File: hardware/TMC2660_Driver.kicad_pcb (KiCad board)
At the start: 4 copper layers, 36.7 x 39.4 mm, 30 parts, among them J1 PCIe_Stepper, J2 Conn_01x04_Male, U1 TMC2660, U2 74LVC1G06, U3 24LC02

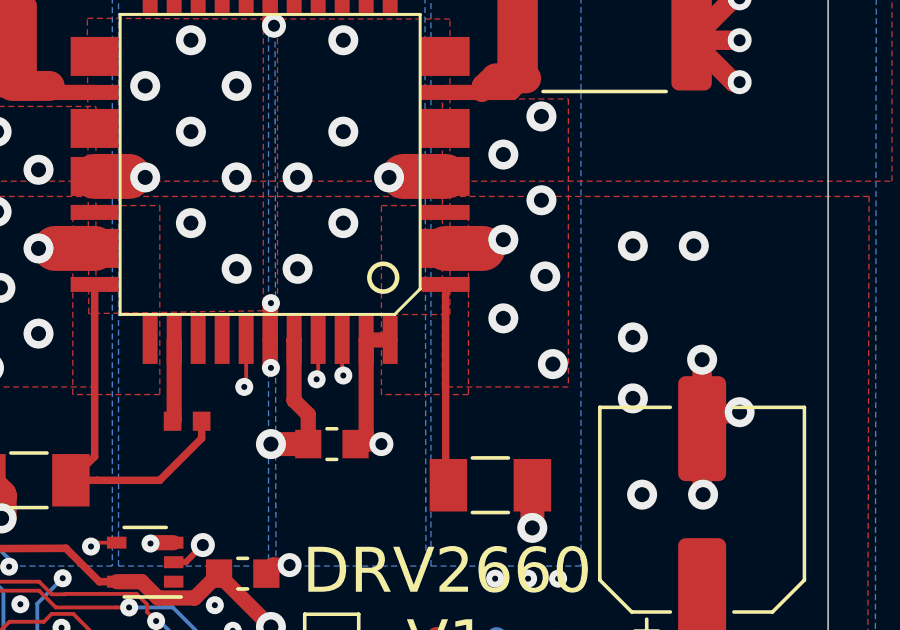
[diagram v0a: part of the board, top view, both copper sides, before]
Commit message: Updated DRC rules. Fix labels.
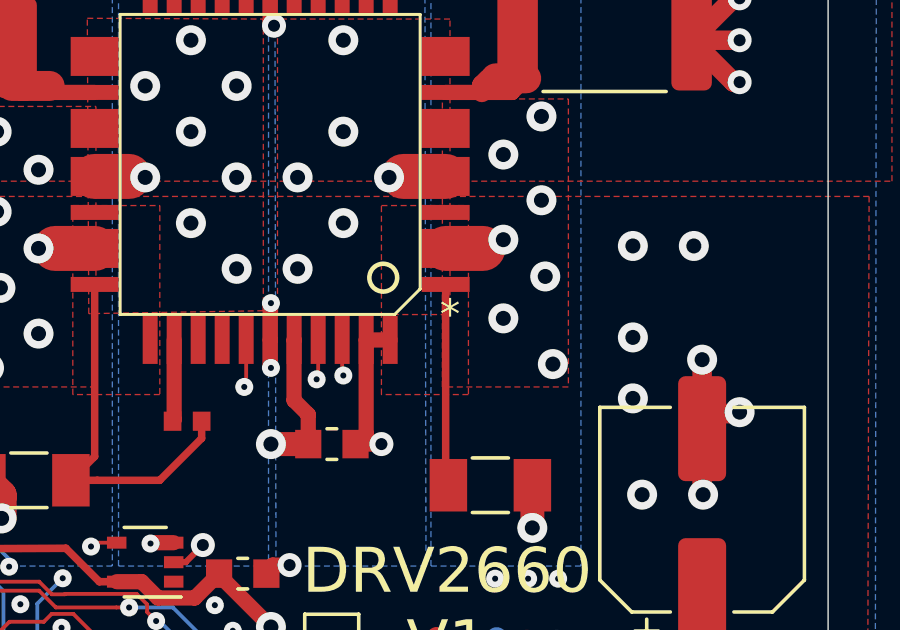
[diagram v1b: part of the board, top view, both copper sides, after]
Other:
- board text added: "(c) iQury.us Nov 2020"
- board text removed: "(c) iQury.us May 2020"
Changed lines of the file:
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@@
     (pcbplotparams
       (layerselection 0x00010fc_ffffffff)
+      (disableapertmacros false)
       (usegerberextensions true)
       (usegerberattributes false)
@@
       (svgprecision 6)
       (excludeedgelayer true)
-      (linewidth 0.100000)
       (plotframeref false)
       (viasonmask false)
@@
   (gr_arc (start 113.6 113) (end 113.6 114) (angle -90) (layer "Edge.Cuts") (width 0.05))
   (gr_line (start 117.5 114) (end 127.7 114) (layer "Edge.Cuts") (width 0.05))
-  (gr_text "(c) iQury.us\nMay 2020" (at 143.637 93 90) (layer "B.SilkS")
+  (gr_text "(c) iQury.us\nNov 2020" (at 143.637 93 90) (layer "B.SilkS")
     (effects (font (size 1 1) (thickness 0.15)) (justify mirror))
   )
@@
     (effects (font (size 1.5 1.5) (thickness 0.3)))
   )
+  (gr_text "*" (at 133.096 94.996) (layer "F.SilkS")
+    (effects (font (size 1 1) (thickness 0.15)))
+  )
   (gr_text "*" (at 115.33 100.254) (layer "F.SilkS")

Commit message: Update 2660 and 2130 driver fab files.
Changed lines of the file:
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@@
     (fp_line (start -3.15 -1.6) (end 3.15 -1.6) (layer "F.Fab") (width 0.1))
     (fp_line (start -3.15 1.6) (end -3.15 -1.6) (layer "F.Fab") (width 0.1))
-    (pad "1" smd roundrect (at -2.9 0 180) (size 1.35 3.35) (layers "F.Cu" "F.Paste" "F.Mask") (roundrect_rratio 0.185185)
+    (pad "1" smd roundrect (at -2.9 0 180) (size 1.35 3.35) (layers "F.Cu" "F.Paste" "F.Mask") (roundrect_rratio 0.1851851851851852)
       (net 17 "Net-(R1-Pad2)"))
-    (pad "2" smd roundrect (at 2.9 0 180) (size 1.35 3.35) (layers "F.Cu" "F.Paste" "F.Mask") (roundrect_rratio 0.185185)
+    (pad "2" smd roundrect (at 2.9 0 180) (size 1.35 3.35) (layers "F.Cu" "F.Paste" "F.Mask") (roundrect_rratio 0.1851851851851852)
       (net 2 "GND"))
     (model "${KISYS3DMOD}/Resistor_SMD.3dshapes/R_2512_6332Metric.wrl"
@@
     (fp_line (start -3.15 -1.6) (end 3.15 -1.6) (layer "F.Fab") (width 0.1))
     (fp_line (start 3.15 1.6) (end -3.15 1.6) (layer "F.Fab") (width 0.1))
-    (pad "1" smd roundrect (at -2.9 0) (size 1.35 3.35) (layers "F.Cu" "F.Paste" "F.Mask") (roundrect_rratio 0.185185)
+    (pad "1" smd roundrect (at -2.9 0) (size 1.35 3.35) (layers "F.Cu" "F.Paste" "F.Mask") (roundrect_rratio 0.1851851851851852)
       (net 18 "Net-(R3-Pad2)"))
-    (pad "2" smd roundrect (at 2.9 0) (size 1.35 3.35) (layers "F.Cu" "F.Paste" "F.Mask") (roundrect_rratio 0.185185)
+    (pad "2" smd roundrect (at 2.9 0) (size 1.35 3.35) (layers "F.Cu" "F.Paste" "F.Mask") (roundrect_rratio 0.1851851851851852)
       (net 2 "GND"))
     (model "${KISYS3DMOD}/Resistor_SMD.3dshapes/R_2512_6332Metric.wrl"

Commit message: Generate fabrication files for Rev 5.
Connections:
- net /~CS renamed /~{CS}
- net /~ENABLE renamed /~{ENABLE}

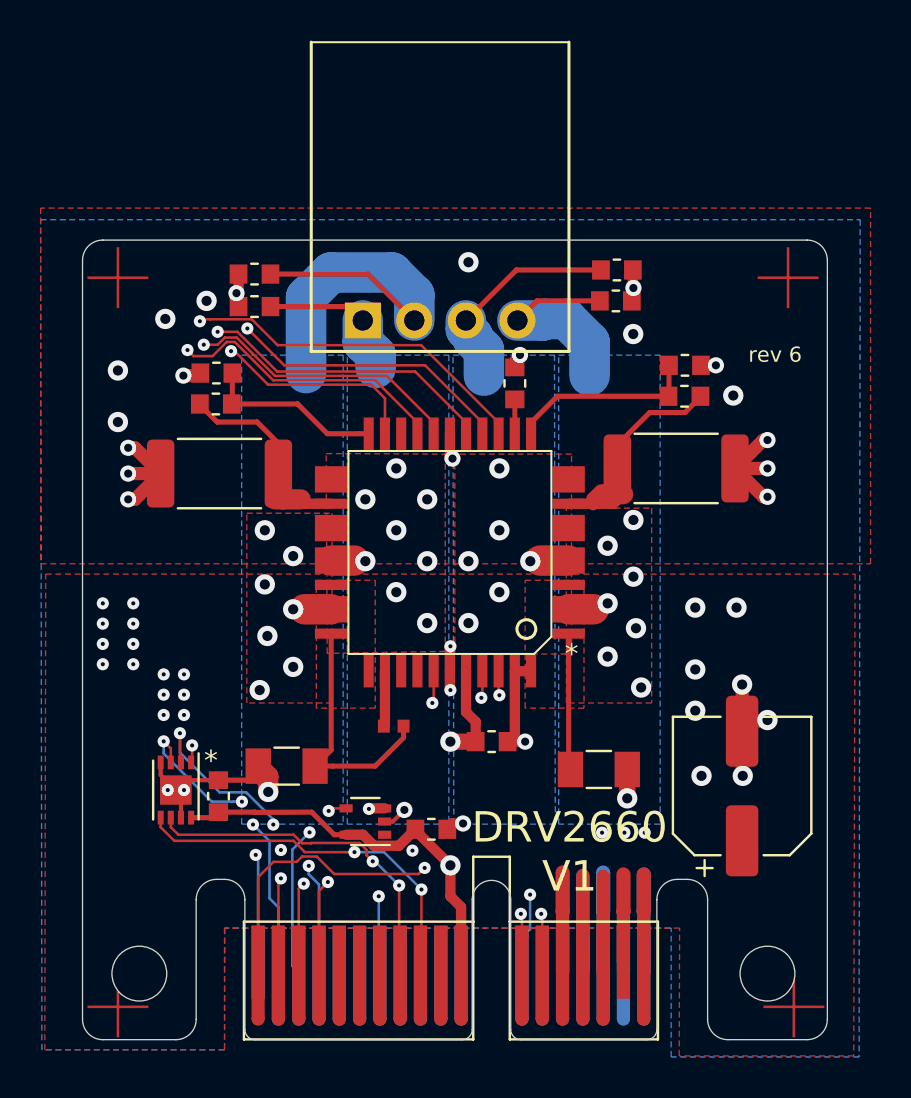
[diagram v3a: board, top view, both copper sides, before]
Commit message: Update drivers to respect high motor coltage circuit.
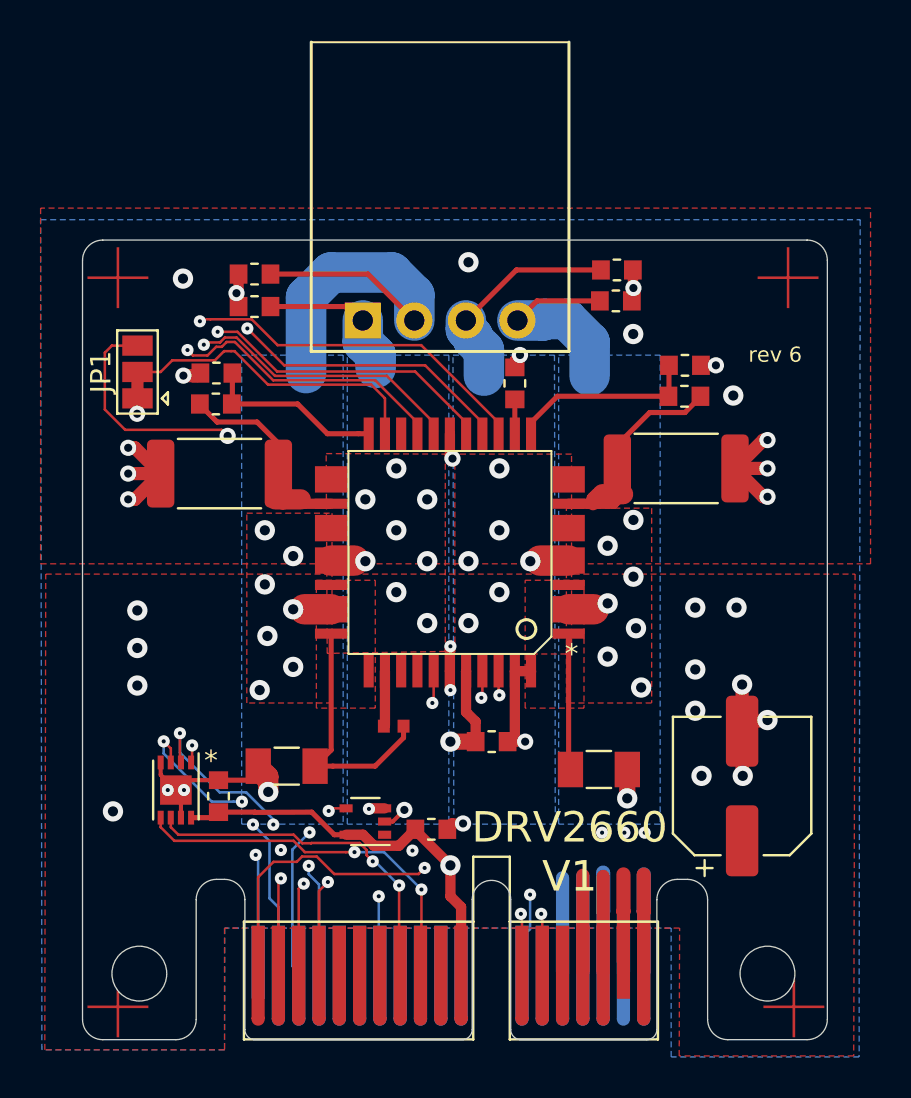
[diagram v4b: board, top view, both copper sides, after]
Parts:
- added JP1: ClkIn, Jumper:SolderJumper-3_P1.3mm_Bridged12_Pad1.0x1.5mm, F.Cu at (111.7, 81.1)
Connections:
- J1 pad B14: /V_MOTORS -> (no net)
- U1 pad 21: /CLOCK -> Net-(U1-Pad21)
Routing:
- net Net-(U1-Pad21): track 0.00 -> 15.3 mm
- net /V_MOTORS: track 43.0 -> 38.1 mm
- net /CLOCK: track 46.2 -> 43.1 mm
- net GND: track 69.1 -> 69.8 mm, vias 53 -> 41
